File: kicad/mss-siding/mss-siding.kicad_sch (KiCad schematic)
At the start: 150 parts, among them J1 Molex 0532610471, J10 Screw_Terminal_01x02, J11 Molex 0532610471, J12 Molex 0532610471, J13 8P8C, J14 SM04B-SRSS, J15 SM04B-SRSS, J16 SM04B-SRSS, J17 SM04B-SRSS, J18 AVR-ISP, J19 Screw_Terminal_01x02, J2 Molex 0532610471, J3 Screw_Terminal_01x02, J4 8P8C, J5 Screw_Terminal_01x02, J6 Screw_Terminal_01x02, J7 Screw_Terminal_01x02, J8 8P8C, J9 Screw_Terminal_01x02, K1 AGQ200A4H, K2 AGQ200A4H, K3 AGQ200A4H, Q1 ZXMS6004FF, Q2 DRDC3105-7, SW1 JS202011SCQN, SW2 JS202011SCQN, U1 AP63205WU, U2 AP3012, U3 74HC4049, U4 74HC4049, U5 PCA9555PW, U6 ATtiny861A-S, U7 WS2812B

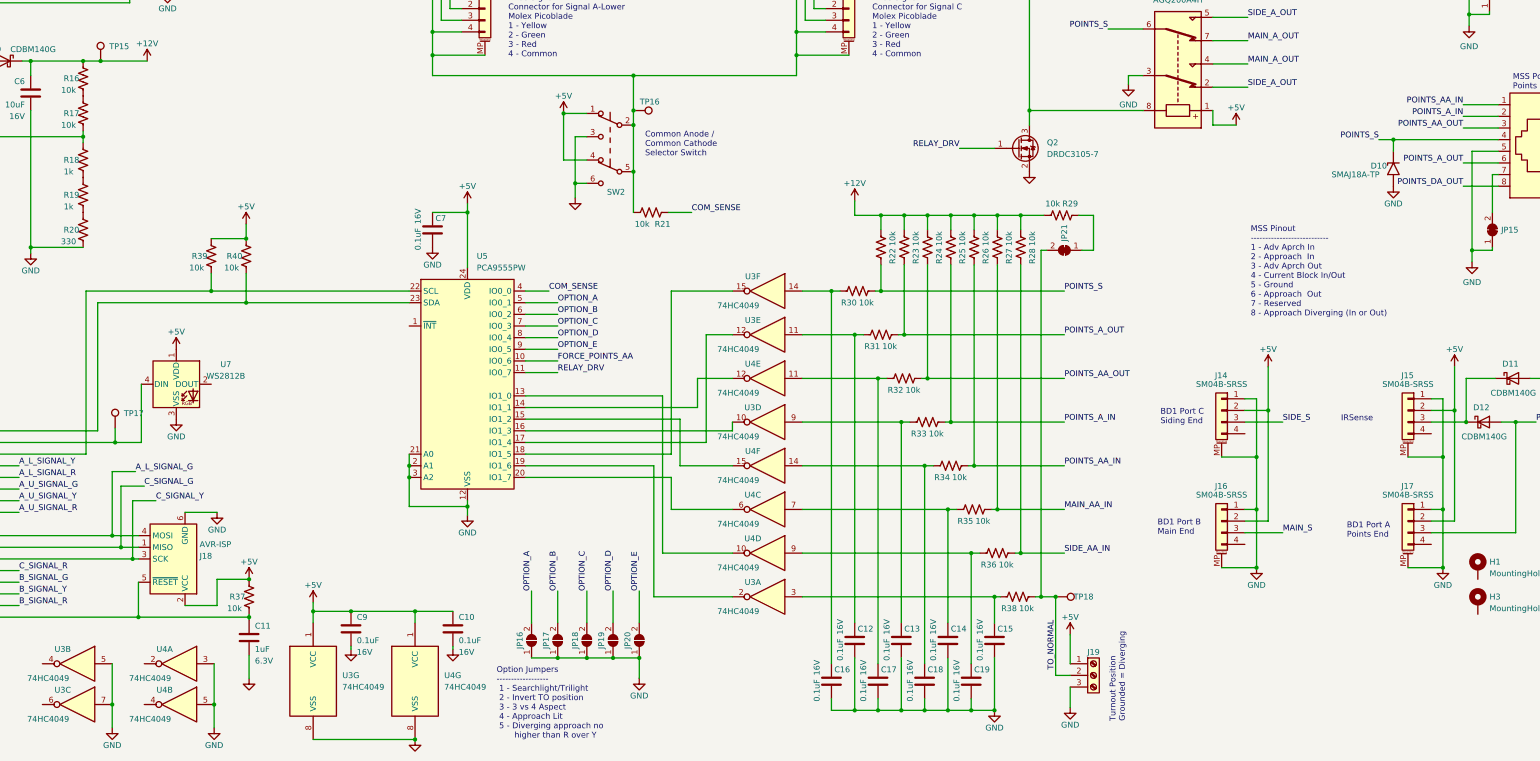
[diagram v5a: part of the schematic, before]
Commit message: Work on v1.1 that adds the lines needed for approach lighting on the frog end.
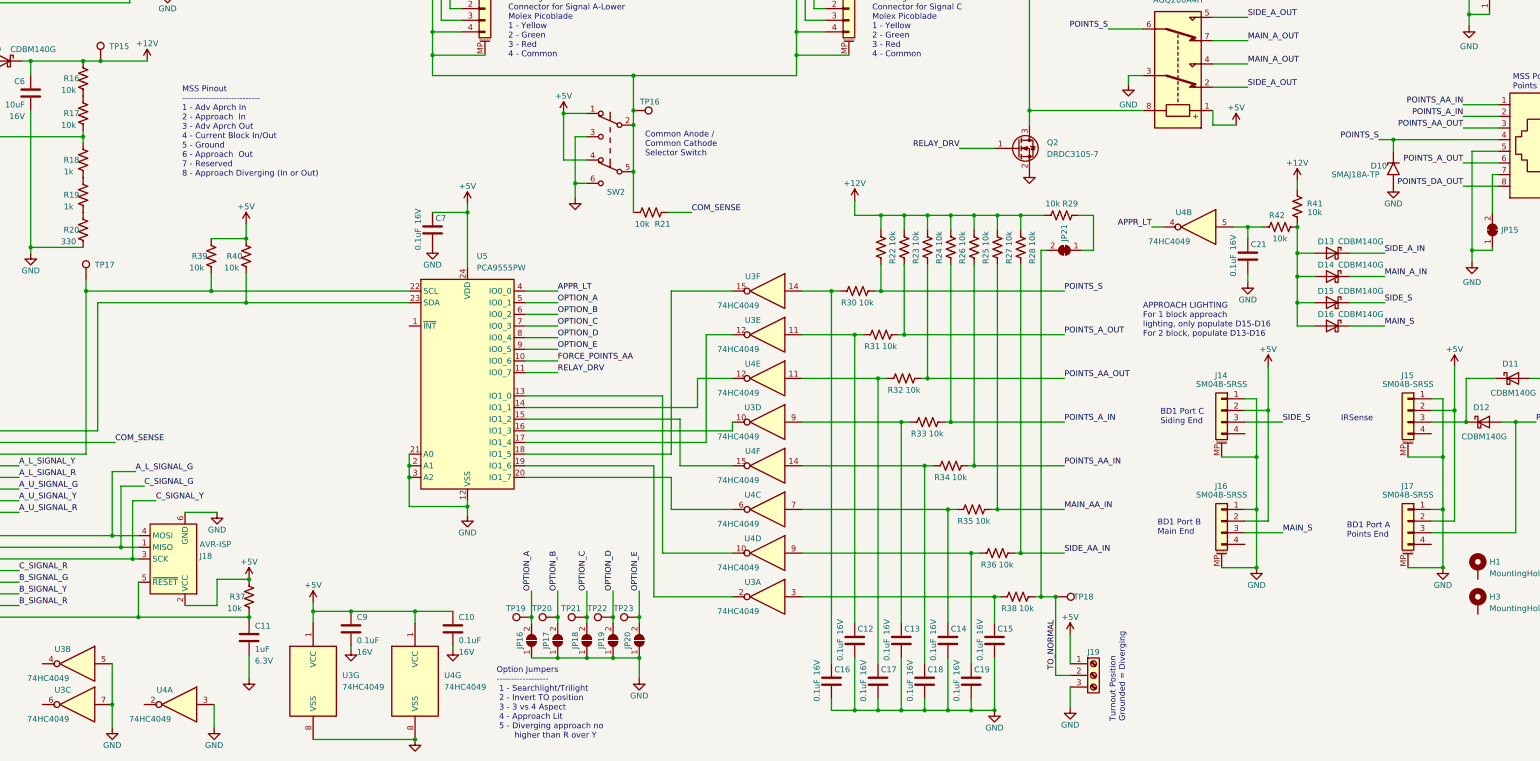
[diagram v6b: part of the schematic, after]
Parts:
- removed unit 1 of U4
- removed U7: WS2812B, LED_SMD:LED_WS2812B_PLCC4_5.0x5.0mm_P3.2mm, symbol LED:WS2812B
- added C21: 0.1uF, Capacitor_SMD:C_0805_2012Metric, symbol Device:C
- added D13, D14, D15, D16: CDBM140G, ISE_Generic:SOD-123T, symbol Device:D_Schottky
- added R41, R42: 10k, Resistor_SMD:R_0805_2012Metric, symbol Device:R_US
- added TP19, TP20, TP21, TP22, TP23: TestPoint, TestPoint:TestPoint_Pad_D2.0mm, symbol Connector:TestPoint
- added unit 2 of U4
- renumbered R26 to R25, R25 to R26
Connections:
- net +12V: now also R41.1
- net COM_SENSE: now also U6.19 (PA1); no longer U5.4 (IO0_0)
- net GND: now also U4.3, C21.2; no longer U4.5
- net MAIN_A_IN: now also D14.1 (K)
- net MAIN_S: now also D16.1 (K)
- net OPTION_A: now also TP19.1
- net OPTION_B: now also TP20.1
- net OPTION_C: now also TP21.1
- net OPTION_D: now also TP22.1
- net OPTION_E: now also TP23.1
- net SIDE_A_IN: now also D13.1 (K)
- net SIDE_S: now also D15.1 (K)
- net at R39.1, U5.22 (SCL), U6.18 (PA2): now also TP17.1
- new net: D13.2 (A), D14.2 (A), D15.2 (A), D16.2 (A), R41.2, R42.1
- new net: C21.1, R42.2, U4.5
- new net APPR_LT: U4.4, U5.4 (IO0_0)
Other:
- note added: "APPROACH LIGHTING For 1 block approach lighting, only populate D15-D16 For 2 block, populate D13-D16"
